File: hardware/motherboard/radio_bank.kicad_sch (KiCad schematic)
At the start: 6 parts, among them J8 RADIO 1-4, J9 RADIO 5-8, U2 AMS1117-3.3

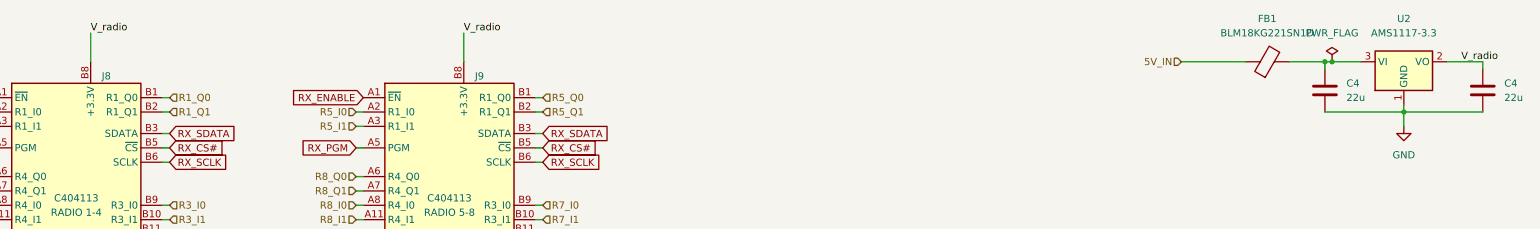
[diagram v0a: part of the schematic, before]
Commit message: Update to KiCAD 10
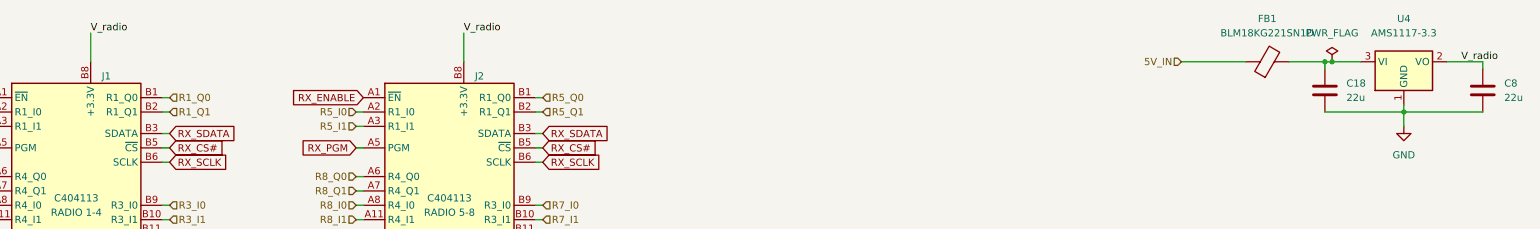
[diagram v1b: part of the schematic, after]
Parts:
- renumbered C4 to C18, C4 to C8, J8 to J1, J9 to J2, U2 to U4
